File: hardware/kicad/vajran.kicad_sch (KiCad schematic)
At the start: 0 parts

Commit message: >
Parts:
- added C1: 10 µF, Capacitor_SMD:C_1206_3216Metric, symbol Device:C_Small
- added C5: 0.1 µF, Capacitor_SMD:C_0603_1608Metric, symbol Device:C_Small
- added IC1: LMR23630AFQDDARQ1, LMR23630AFQDDARQ1:SOIC127P600X170-9N, symbol LMR23630AFQDDARQ1:LMR23630AFQDDARQ1
- added L3: SRN6045TA-150M, Inductor_SMD:L_Bourns_SRN6045TA, symbol SRN6045TA-150M:SRN6045TA-150M
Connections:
- new net: C5.1, IC1.1 (SW)
- new net: C5.2, IC1.2 (BOOT)
- new net +24V: C1.1, IC1.5 (EN/SYNC), IC1.7 (VIN)
- new net GND: C1.2

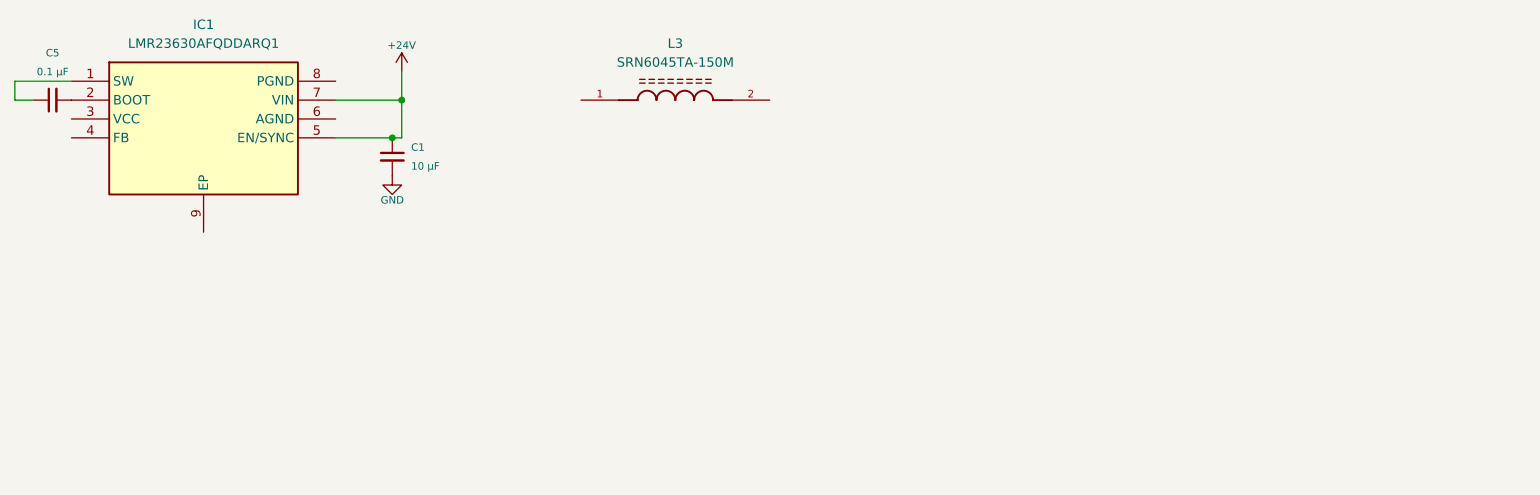
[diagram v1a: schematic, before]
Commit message: added 24v to 5v
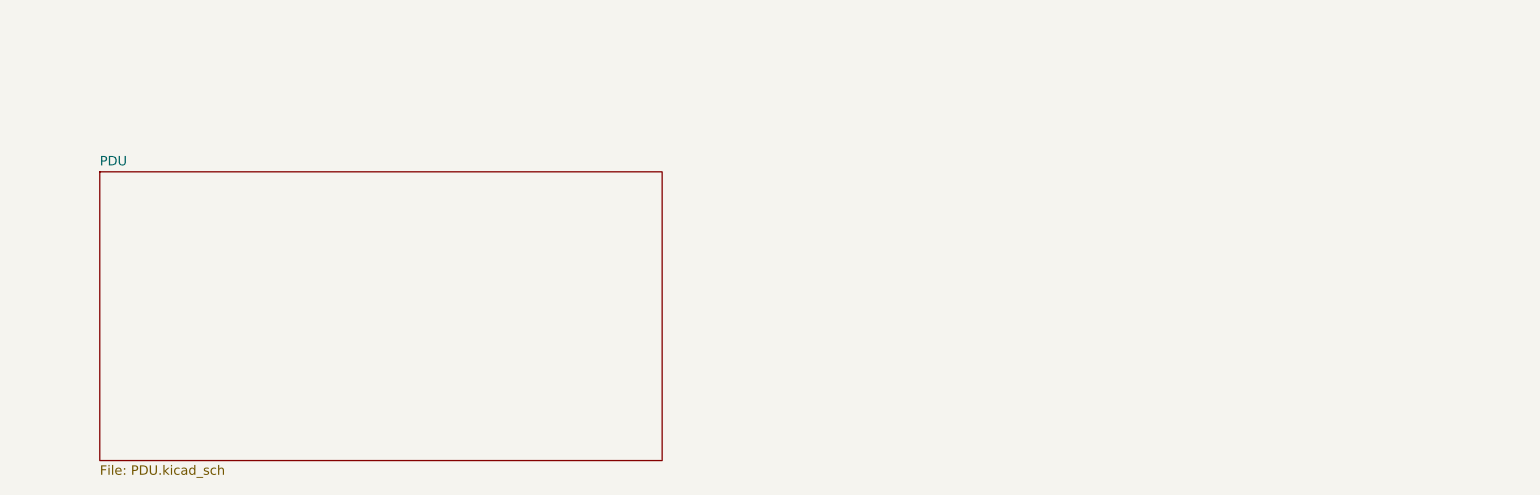
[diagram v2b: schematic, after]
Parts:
- removed C1: 10 µF, Capacitor_SMD:C_1206_3216Metric, symbol Device:C_Small
- removed C5: 0.1 µF, Capacitor_SMD:C_0603_1608Metric, symbol Device:C_Small
- removed IC1: LMR23630AFQDDARQ1, LMR23630AFQDDARQ1:SOIC127P600X170-9N, symbol LMR23630AFQDDARQ1:LMR23630AFQDDARQ1
- removed L3: SRN6045TA-150M, Inductor_SMD:L_Bourns_SRN6045TA, symbol SRN6045TA-150M:SRN6045TA-150M
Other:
- added sheet PDU (PDU.kicad_sch)

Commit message: updated
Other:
- added sheet COMMUNICATION (COMM.kicad_sch)
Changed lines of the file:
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@@
 			(effects
 				(font
+					(face "Courier New")
 					(size 1.27 1.27)
 				)
@@
 				)
 			)
+		)
+	)
+	(sheet
+		(at 174.498 55.626)
+		(size 80.772 38.608)
+		(exclude_from_sim no)
+		(in_bom yes)
+		(on_board yes)
+		(dnp no)
+		(fields_autoplaced yes)
+		(stroke
+			(width 0.1524)
+			(type solid)
+		)
+		(fill
+			(color 0 0 0 0)
+		)
+		(property "Sheetname" "COMMUNICATION"
+			(at 174.498 54.9144 0)
+			(show_name no)
+			(do_not_autoplace no)
+			(effects
+				(font
+					(size 1.27 1.27)
+				)
+				(justify left bottom)
+			)
+		)
+		(property "Sheetfile" "COMM.kicad_sch"
+			(at 174.498 94.8186 0)
+			(show_name no)
+			(do_not_autoplace no)
+			(effects
+				(font
+					(size 1.27 1.27)
+				)
+				(justify left top)
+			)
+		)
+		(instances
+			(project "vajran"
+				(path "/7388b7ed-711f-4089-9af6-82932916e4d0"
+					(page "3")
+				)
+			)
